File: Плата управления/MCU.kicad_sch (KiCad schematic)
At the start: 19 parts, among them U6 ASEMB-10, U7 APM32F405xG

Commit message: Развел все длорожки
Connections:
- net Enable: no longer names the net of U7.37 (PB2)
- no-connect marks 58 -> 59
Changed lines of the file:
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@@
+	)
+	(no_connect
+		(at 106.68 95.885)
 	)
 	(no_connect
@@
 			(effects
 				(font
-					(size 1.27 1.27)
-				)
-				(justify left)
-				(hide yes)
-			)
-		)
-	)
-	(global_label "Enable"
-		(shape input)
-		(at 106.68 95.885 0)
-		(fields_autoplaced yes)
-		(effects
-			(font
-				(size 1.27 1.27)
-			)
-			(justify left)
-		)
-		(property "Intersheetrefs" "${INTERSHEET_REFS}"
-			(at 115.9356 95.885 0)
-			(effects
-				(font

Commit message: Добавил разъёмф для крепления
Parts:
- added C56, C57: 0.1u, Capacitor_SMD:C_0603_1608Metric_Pad1.08x0.95mm_HandSolder, symbol Device:C_Small
- added R26: 0, Resistor_SMD:R_0603_1608Metric_Pad0.98x0.95mm_HandSolder, symbol Device:R_Small
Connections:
- net Current_A_MCU: now also U7.30 (PA5); no longer U7.29 (PA4)
- net Current_B_MCU: now also U7.31 (PA6); no longer U7.30 (PA5)
- net Current_C_MCU: now also U7.32 (PA7); no longer U7.31 (PA6)
- net GND: now also C56.1, C57.2
- net at U6.3 (Out), U7.12 (PH0): now also C56.2
- net at U7.13 (PH1): now also R26.2
- net PCB_Temp_A_MCU: now reaches U7.25 (PA2)
- net PCB_Temp_B_MCU: now reaches U7.26 (PA3)
- net at U6.1 (Standby): now also C57.1, R26.1
- net PCB_Temp_MCU: no longer names the net of U7.35 (PB0)
- new net PCB_Temp_C_MCU: U7.29 (PA4)
- no-connect marks 59 -> 55
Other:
- moved on the sheet: C16, U6

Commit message: Добавил модель плты
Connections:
- net PCB_Temp_C_MCU: now also U7.35 (PB0); no longer U7.29 (PA4)
- new net DAC_OUT1: U7.29 (PA4)
- no-connect marks 55 -> 54

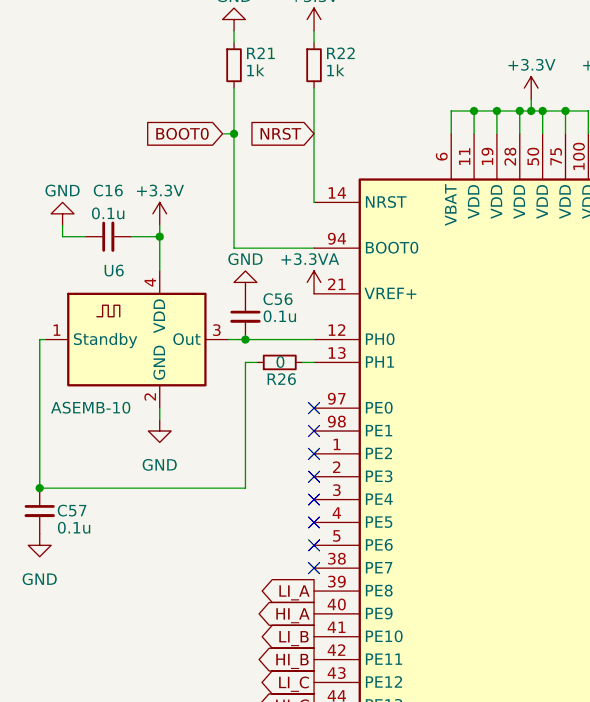
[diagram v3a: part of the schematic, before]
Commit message: Добавил все в BOM
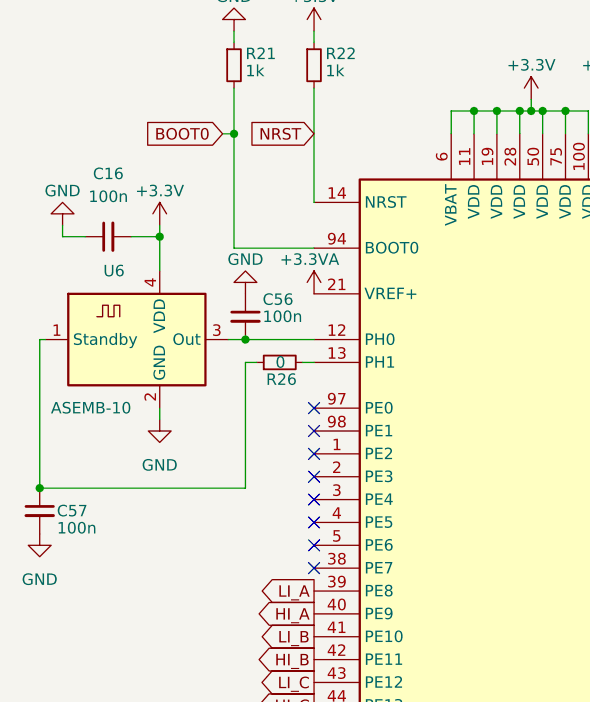
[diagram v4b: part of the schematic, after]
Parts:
- C16, C56, C57: value 0.1u -> 100n
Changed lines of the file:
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@@
 		(fields_autoplaced yes)
 		(property "Reference" "C16"
-			(at 38.1063 46.355 90)
-			(effects
-				(font
-					(size 1.27 1.27)
-				)
-			)
-		)
-		(property "Value" "0.1u"
-			(at 38.1063 48.895 90)
+			(at 38.1063 44.45 90)
+			(effects
+				(font
+					(size 1.27 1.27)
+				)
+			)
+		)
+		(property "Value" "100n"
+			(at 38.1063 46.99 90)
 			(effects
 				(font
@@
 			)
 		)
-		(property "Value" "0.1u"
+		(property "Value" "100n"
 			(at 32.385 83.82 0)
 			(effects
@@
 			)
 		)
-		(property "Value" "0.1u"
+		(property "Value" "100n"
 			(at 55.245 60.325 0)
 			(effects

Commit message: Изменения: добавил папку с отчетностью
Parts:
- added R27: 0, Resistor_SMD:R_0603_1608Metric_Pad0.98x0.95mm_HandSolder, symbol Device:R_Small
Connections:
- net +3.3V: now also R27.2; no longer U6.4 (VDD)
- new net: R27.1, U6.4 (VDD)
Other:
- moved on the sheet: C16
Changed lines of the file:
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@@
 	(paper "A4")
 	(title_block
-		(comment 1 "МПСТ.76721.758764.02.Э3.М")
+		(comment 1 "МПСТ.6319.758764.02.Э3.М")
+	)
+	(junction
+		(at 43.815 50.165)
+		(diameter 0)
+		(color 0 0 0 0)
 	)
 	(junction
@@
 	)
 	(junction
-		(at 43.815 51.435)
-		(diameter 0)
-		(color 0 0 0 0)
-	)
-	(junction
 		(at 248.92 64.77)
 		(diameter 0)
@@
 	(wire
 		(pts
-			(xy 88.9 37.465) (xy 91.44 37.465)
+			(xy 40.64 50.165) (xy 43.815 50.165)
 		)
 		(stroke
@@
 	(wire
 		(pts
-			(xy 52.07 34.925) (xy 52.07 40.005)
+			(xy 88.9 37.465) (xy 91.44 37.465)
 		)
 		(stroke
@@
 	(wire
 		(pts
-			(xy 82.55 182.245) (xy 82.55 184.785)
+			(xy 52.07 34.925) (xy 52.07 40.005)
 		)
 		(stroke
@@
 	(wire
 		(pts
-			(xy 43.815 51.435) (xy 43.815 55.245)
+			(xy 82.55 182.245) (xy 82.55 184.785)
 		)
 		(stroke
@@
 	(wire
 		(pts
-			(xy 40.64 51.435) (xy 43.815 51.435)
-		)
-		(stroke
-			(width 0)
-			(type default)
-		)
-	)
-	(wire
-		(pts
 			(xy 93.98 36.195) (xy 93.98 40.005)
 		)
@@
 	(wire
 		(pts
-			(xy 33.02 51.435) (xy 35.56 51.435)
+			(xy 33.02 50.165) (xy 35.56 50.165)
 		)
 		(stroke
@@
 	(wire
 		(pts
-			(xy 33.02 50.165) (xy 33.02 51.435)
-		)
-		(stroke
-			(width 0)
-			(type default)
-		)
-	)
-	(wire
-		(pts
 			(xy 279.4 50.8) (xy 279.4 52.07)
 		)
@@
 	(wire
 		(pts
-			(xy 43.815 50.165) (xy 43.815 51.435)
-		)
-		(stroke
-			(width 0)
-			(type default)
-		)
-	)
-	(wire
-		(pts
 			(xy 248.92 30.48) (xy 248.92 31.75)
 		)
@@
 	(symbol
 		(lib_id "Device:C_Small")
-		(at 38.1 51.435 90)
+		(at 38.1 50.165 90)
 		(unit 1)
 		(exclude_from_sim no)
@@
 		(on_board yes)
 		(dnp no)
-		(fields_autoplaced yes)
 		(property "Reference" "C16"
-			(at 38.1063 44.45 90)
+			(at 38.1 46.99 90)
 			(effects
 				(font
@@
 		)
 		(property "Value" "100n"
-			(at 38.1063 46.99 90)
+			(at 38.1 53.34 90)
 			(effects
 				(font
@@
 		)
 		(property "Footprint" "Capacitor_SMD:C_0603_1608Metric_Pad1.08x0.95mm_HandSolder"
-			(at 38.1 51.435 0)
+			(at 38.1 50.165 0)
 			(effects
 				(font
@@
 		)
 		(property "Datasheet" "~"
-			(at 38.1 51.435 0)
+			(at 38.1 50.165 0)
 			(effects
 				(font
@@
 		)
 		(property "Description" ""
-			(at 38.1 51.435 0)
+			(at 38.1 50.165 0)
 			(effects
 				(font
@@
 		(dnp no)
 		(property "Reference" "R26"
-			(at 59.055 67.31 90)
+			(at 58.42 67.31 90)
 			(effects
 				(font
@@
 	)
 	(symbol
+		(lib_id "Device:R_Small")
+		(at 43.815 52.705 180)
+		(unit 1)
+		(exclude_from_sim no)
+		(in_bom yes)
+		(on_board yes)
+		(dnp no)
+		(property "Reference" "R27"
+			(at 45.72 51.435 90)
+			(effects
+				(font
+					(size 1.27 1.27)
+				)
+				(justify left)
+			)
+		)
+		(property "Value" "0"
+			(at 43.815 52.07 90)
+			(effects
+				(font
+					(size 1.27 1.27)
+				)
+				(justify left)
+			)
+		)
+		(property "Footprint" "Resistor_SMD:R_0603_1608Metric_Pad0.98x0.95mm_HandSolder"
+			(at 43.815 52.705 0)
+			(effects
+				(font
+					(size 1.27 1.27)
+				)
+				(hide yes)
+			)
+		)
+		(property "Datasheet" "~"
+			(at 43.815 52.705 0)
+			(effects
+				(font
+					(size 1.27 1.27)
+				)
+				(hide yes)
+			)
+		)
+		(property "Description" ""
+			(at 43.815 52.705 0)
+			(effects
+				(font
+					(size 1.27 1.27)
+				)
+				(hide yes)
+			)
+		)
+		(pin "1"
+		)
+		(pin "2"
+		)
+		(instances
+			(project "Плата управления"
+				(path "/75f4c67c-bbde-4446-8f82-67797a1b269f/5edc1bc4-8927-4ae0-9f52-ef5d9c5bfa46"
+					(reference "R27")
+					(unit 1)
+				)
+			)
+		)
+	)
+	(symbol
 		(lib_id "Device:C_Small")
 		(at 248.92 68.58 0)
@@
 		(dnp no)
 		(property "Reference" "U6"
-			(at 38.735 55.245 0)
+			(at 34.925 56.515 0)
 			(effects
 				(font
@@
 		)
 		(property "Value" "ASEMB-10"
-			(at 36.195 70.485 0)
+			(at 37.465 69.215 0)
 			(effects
 				(font
 					(size 1.27 1.27)
 				)
+				(hide yes)
 			)
 		)
